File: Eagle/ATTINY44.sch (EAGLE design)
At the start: 8 parts, among them IC1 TINY85

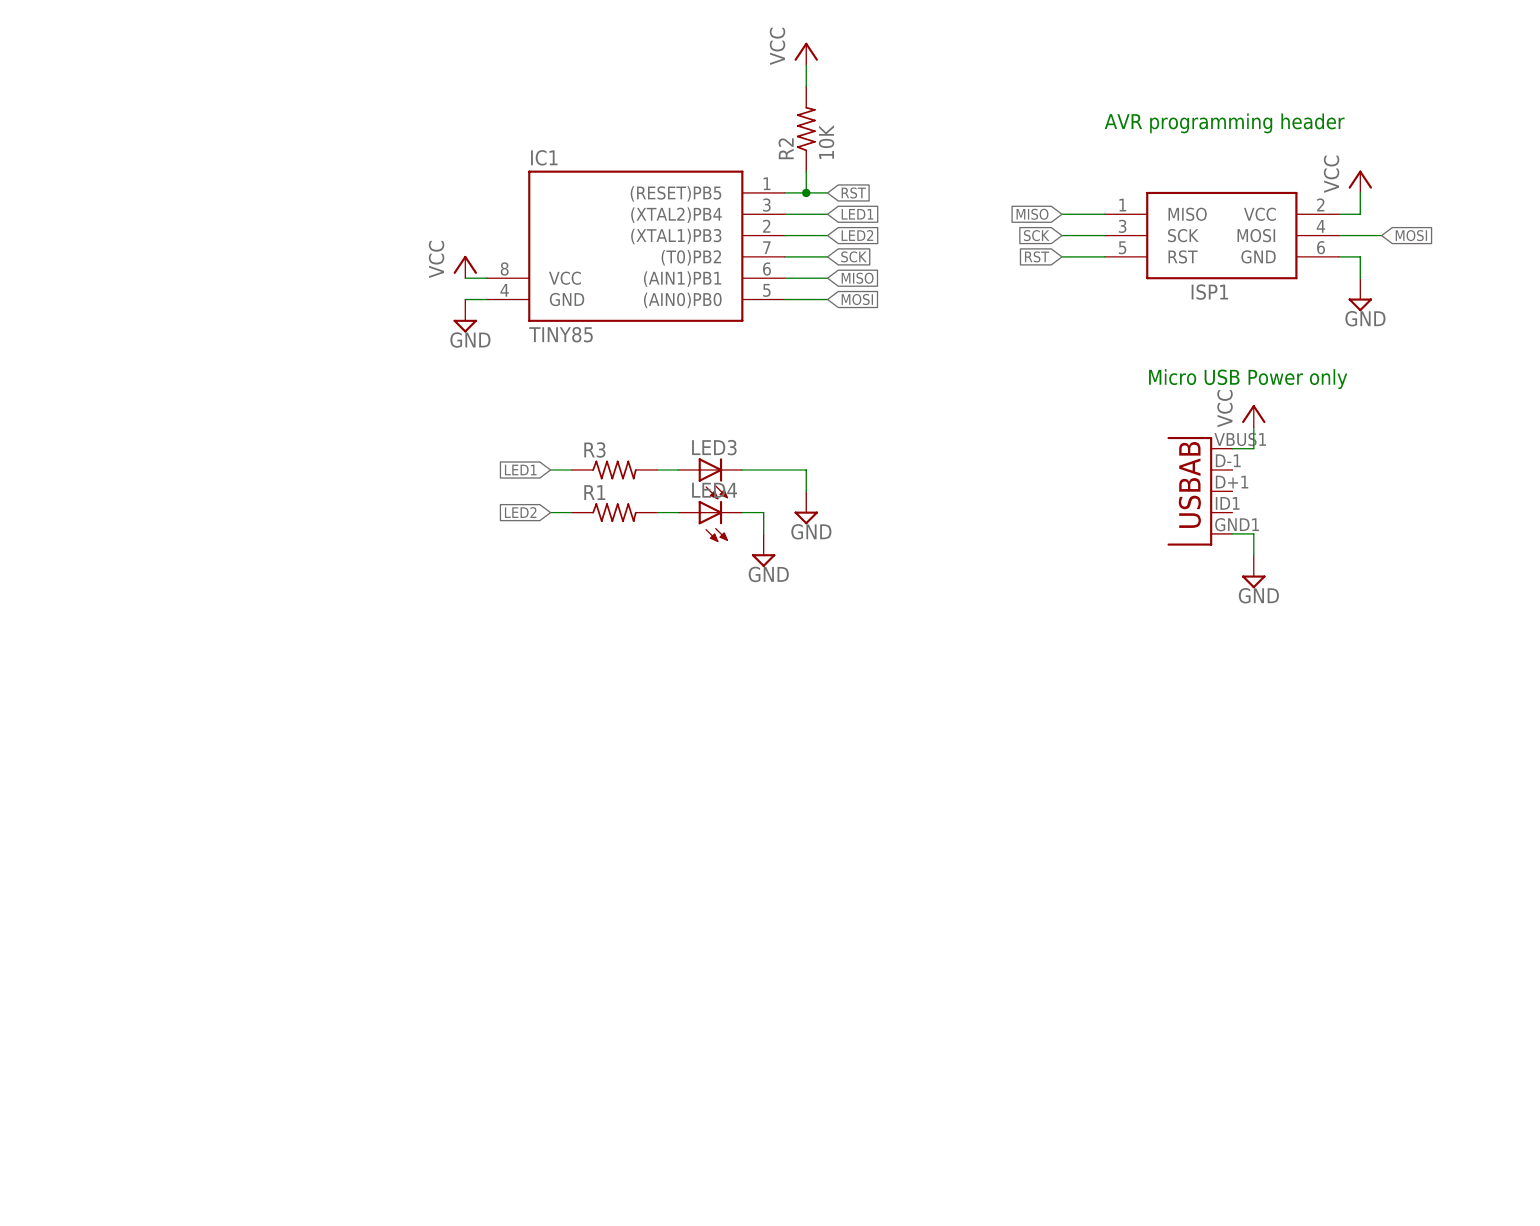
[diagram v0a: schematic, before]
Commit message: Added ATTINY44 breakout board
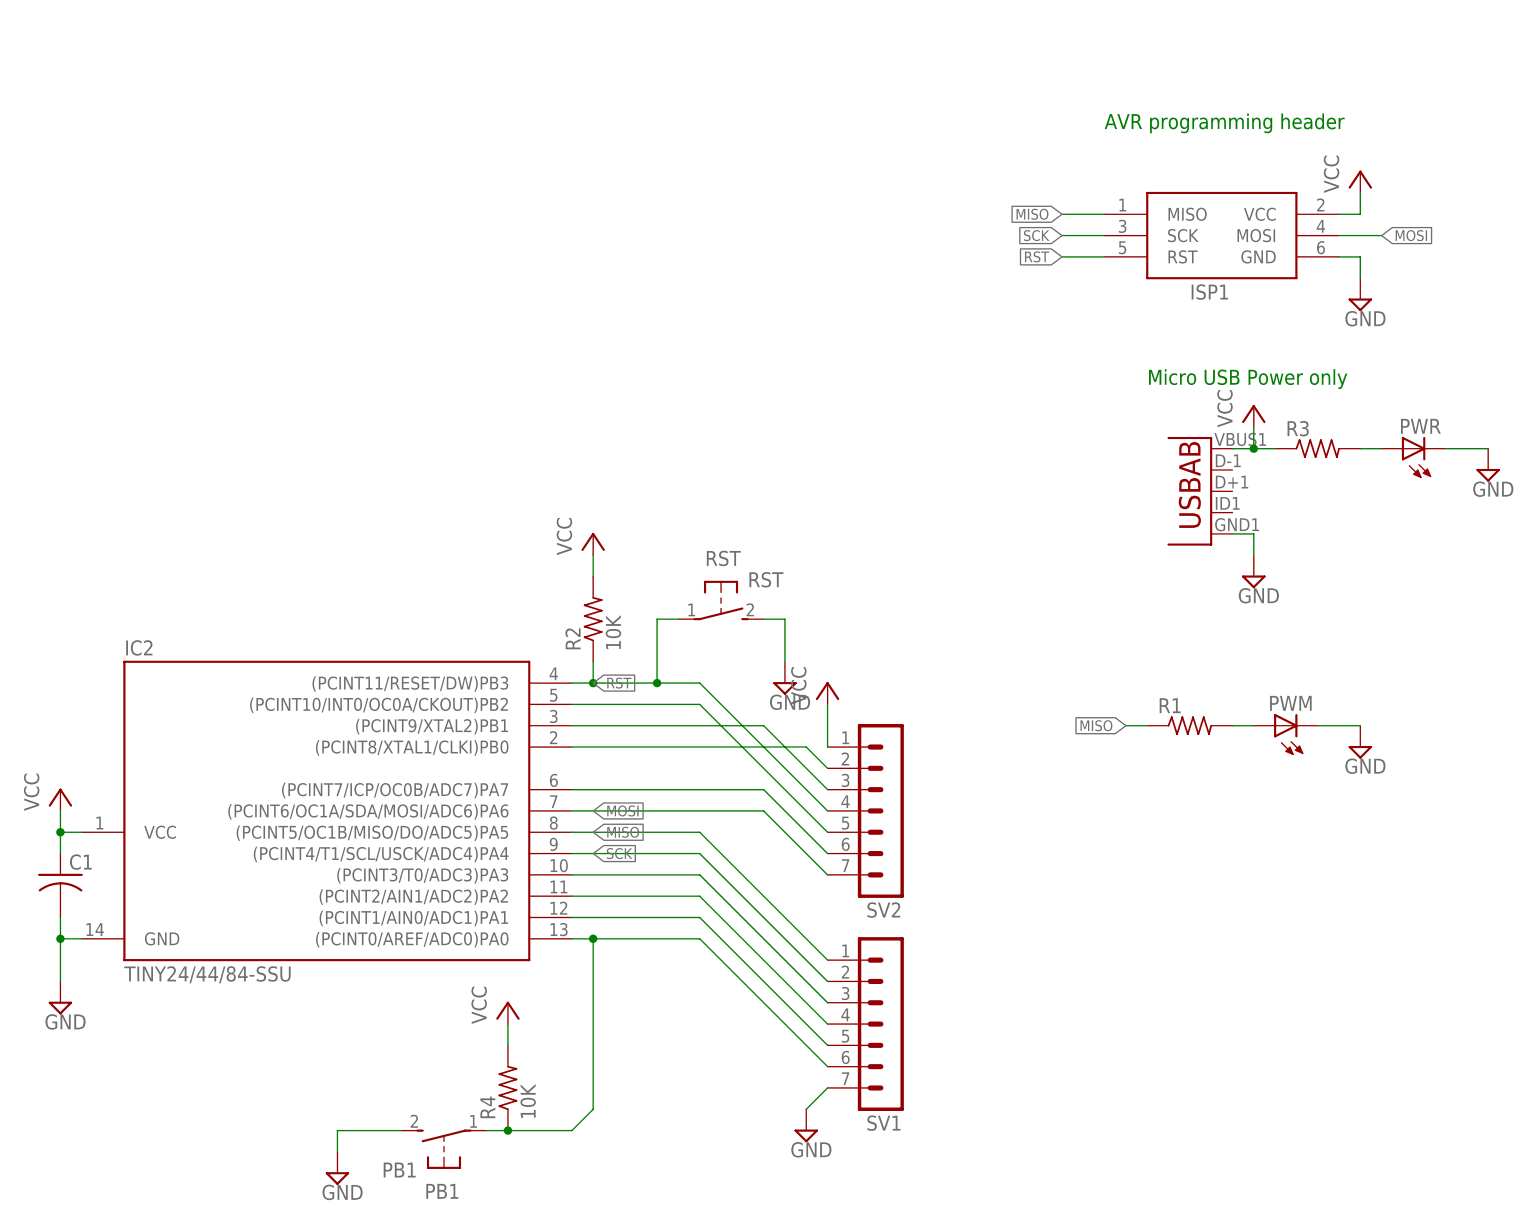
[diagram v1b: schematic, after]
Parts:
- removed IC1: TINY85, atmel:TINY10S
- removed LED3, LED4: (no value), adafruit:LEDCHIPLED_0805
- added C1: (no value), rcl:C-USC0805
- added IC2: TINY24/44/84-SSU, avr-5:TINY24/44/84-SSU
- added PB1: PB1, switch-tact:DTSM-3
- added PWM, PWR: (no value), adafruit:LEDCHIPLED_0805
- added R4: 10K, rcl:R-US_R0805
- added RST: RST, switch-tact:DTSM-3
- added SV1, SV2: (no value), con-lstb:MA07-1
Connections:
- removed net LED1: IC1.(XTAL2)PB4, R3.1
- removed net LED2: IC1.(XTAL1)PB3, R1.1
- new net N$3: IC2.(PCINT8/XTAL1/CLKI)PB0, SV2.2
- new net N$4: IC2.(PCINT9/XTAL2)PB1, SV2.3
- new net N$5: IC2.(PCINT10/INT0/OC0A/CKOUT)PB2, SV2.5
- new net N$6: IC2.(PCINT7/ICP/OC0B/ADC7)PA7, SV2.6
- new net PIN10: IC2.(PCINT3/T0/ADC3)PA3, SV1.3
- new net PIN11: IC2.(PCINT2/AIN1/ADC2)PA2, SV1.4
- new net PIN12: IC2.(PCINT1/AIN0/ADC1)PA1, SV1.5
- new net PIN13: IC2.(PCINT0/AREF/ADC0)PA0, PB1.1, R4.1, SV1.6
- net GND: now also C1.2, IC2.GND, PB1.2, PWM.C, PWR.C, RST.2, SV1.7; no longer IC1.GND, LED3.C, LED4.C
- net MISO: now also IC2.(PCINT5/OC1B/MISO/DO/ADC5)PA5, R1.1, SV1.1; no longer IC1.(AIN1)PB1
- net MOSI: now also IC2.(PCINT6/OC1A/SDA/MOSI/ADC6)PA6, SV2.7; no longer IC1.(AIN0)PB0
- net N$1: now also PWR.A; no longer LED3.A
- net N$2: now also PWM.A; no longer LED4.A
- net RST: now also IC2.(PCINT11/RESET/DW)PB3, RST.1, SV2.4; no longer IC1.(RESET)PB5
- net SCK: now also IC2.(PCINT4/T1/SCL/USCK/ADC4)PA4, SV1.2; no longer IC1.(T0)PB2
- net VCC: now also C1.1, IC2.VCC, R3.1, R4.2, SV2.1; no longer IC1.VCC
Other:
- moved on the sheet: R1, R2, R3
